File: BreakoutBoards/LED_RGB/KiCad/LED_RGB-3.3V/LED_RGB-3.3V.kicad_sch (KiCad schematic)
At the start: 1 part

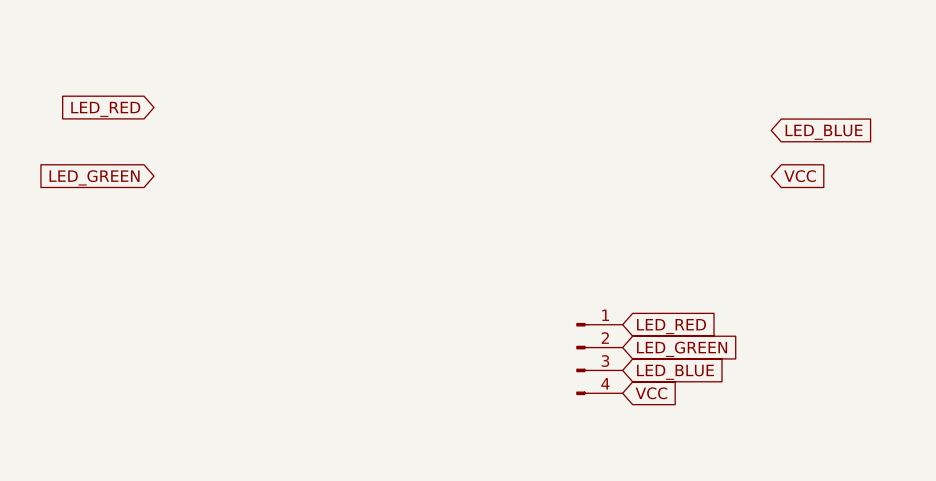
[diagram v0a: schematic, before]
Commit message: updated to Mk1 and sent for manufacturing
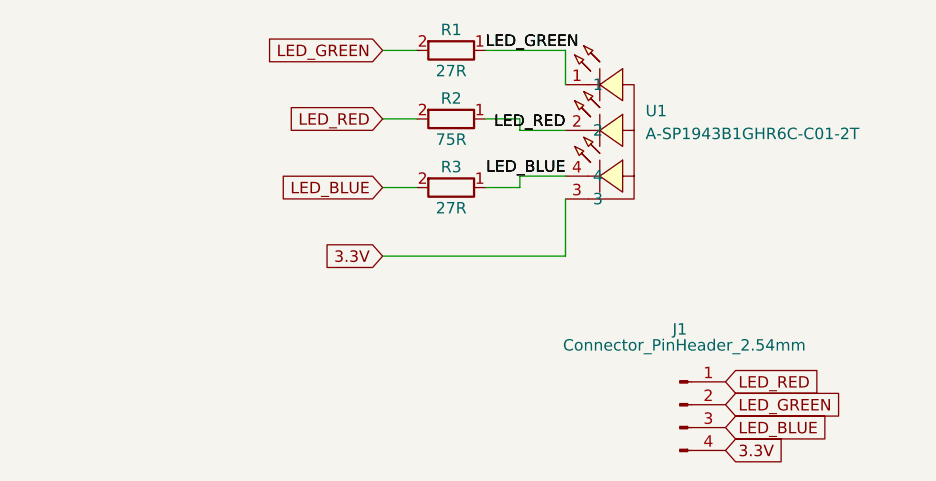
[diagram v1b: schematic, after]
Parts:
- added R1, R3: 27R, clectric-diy:R0603, symbol Device:R
- added R2: 75R, clectric-diy:R0603, symbol Device:R
- added U1: A-SP1943B1GHR6C-C01-2T, clectric-diy:LED-SMD_4P-L1.6-W1.5-BL_A-SP1943B1GHR6C-C01-2T, symbol clectric-diy:A-SP1943B1GHR6C-C01-2T
- J1: value ~ -> Connector_PinHeader_2.54mm
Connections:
- net LED_BLUE: now also R3.1, R3.2, U1.4
- net LED_GREEN: now also R1.1, R1.2, U1.1
- net LED_RED: now also R2.1, R2.2, U1.2
- net VCC renamed 3.3V
- net 3.3V: now also U1.3
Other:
- title: Charge LED_RGB -> Charge 3.3V RGB LED
